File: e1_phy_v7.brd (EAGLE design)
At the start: 100 x 75 mm, 136 parts, among them IC2 LD117AS33TR, IC3 LD117AS33TR, IC4 MCP4725, U1 XRT82D20, U2 GPS_GNS_2201, U3 VCTCXO-CONNORWINFIELD, U4 VCXO_TAITIEN_VT, X2 SMA-142-0701-801/806, X3 JACK2.5_SJ-2523, X4 0446200002

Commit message: Pullup on i2c, ERASE jumper.
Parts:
- JP2: device jumper:JP1 -> jumper@1:JP1
- SV4: device con-lstb:MA08-2 -> con-lstb@1:MA08-2
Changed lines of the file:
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@@
 <?xml version="1.0" encoding="utf-8"?>
 <!DOCTYPE eagle SYSTEM "eagle.dtd">
-<eagle version="9.0.1">
+<eagle version="7.7.0">
 <drawing>
 <settings>
 <setting alwaysvectorfont="no"/>
-<setting keepoldvectorfont="yes"/>
 <setting verticaltext="up"/>
 </settings>
@@
 <attribute name="VALUE" x="43.65625" y="36.86175" size="0.0254" layer="27"/>
 </element>
-<element name="SV4" library="con-lstb" library_urn="urn:adsk.eagle:library:162" package="MA08-2" package3d_urn="urn:adsk.eagle:package:8335/1" value="" x="69.85" y="13.97" smashed="yes" rot="R90">
+<element name="SV4" library="con-lstb@1" package="MA08-2" value="" x="69.85" y="13.97" smashed="yes" rot="R90">
 <attribute name="MF" value="" x="69.85" y="13.97" size="1.778" layer="27" rot="R90" display="off"/>
 <attribute name="MPN" value="" x="69.85" y="13.97" size="1.778" layer="27" rot="R90" display="off"/>
@@
 <attribute name="TP_SIGNAL_NAME" value="" x="25.4" y="64.77" size="1.778" layer="27" font="vector" display="off"/>
 </element>
-<element name="X4" library="con-molex" library_urn="urn:adsk.eagle:library:165" package="0446200002" value="0446200002" x="4.7625" y="15.24" smashed="yes" rot="R270">
+<element name="X4" library="con-molex" package="0446200002" value="0446200002" x="4.7625" y="15.24" smashed="yes" rot="R270">
 <attribute name="MF" value="MOLEX" x="4.7625" y="15.24" size="1.778" layer="27" font="vector" rot="R270" display="off"/>
 <attribute name="MPN" value="0446200002" x="4.7625" y="15.24" size="1.778" layer="27" font="vector" rot="R270" display="off"/>
@@
 <attribute name="VALUE" x="60.6425" y="51.435" size="1.27" layer="27" rot="R90"/>
 </element>
-<element name="JP2" library="jumper" library_urn="urn:adsk.eagle:library:252" package="JP1" package3d_urn="urn:adsk.eagle:package:15455/1" value="" x="20.32" y="34.29" rot="R270"/>
+<element name="JP2" library="jumper@1" package="JP1" value="" x="20.32" y="34.29" rot="R270"/>
 </elements>
 <signals>
@@
 which will not be processed correctly with this version.
 </note>
-<note version="8.2" severity="warning">
-Since Version 8.2, EAGLE supports online libraries. The ids
-of those online libraries will not be understood (or retained)
-with this version.
-</note>
-<note version="8.3" severity="warning">
-Since Version 8.3, EAGLE supports URNs for individual library
-assets (packages, symbols, and devices). The URNs of those assets
-will not be understood (or retained) with this version.
-</note>
-<note version="8.3" severity="warning">
-Since Version 8.3, EAGLE supports the association of 3D packages
-with devices in libraries, schematics, and board files. Those 3D
-packages will not be understood (or retained) with this version.
-</note>
 </compatibility>

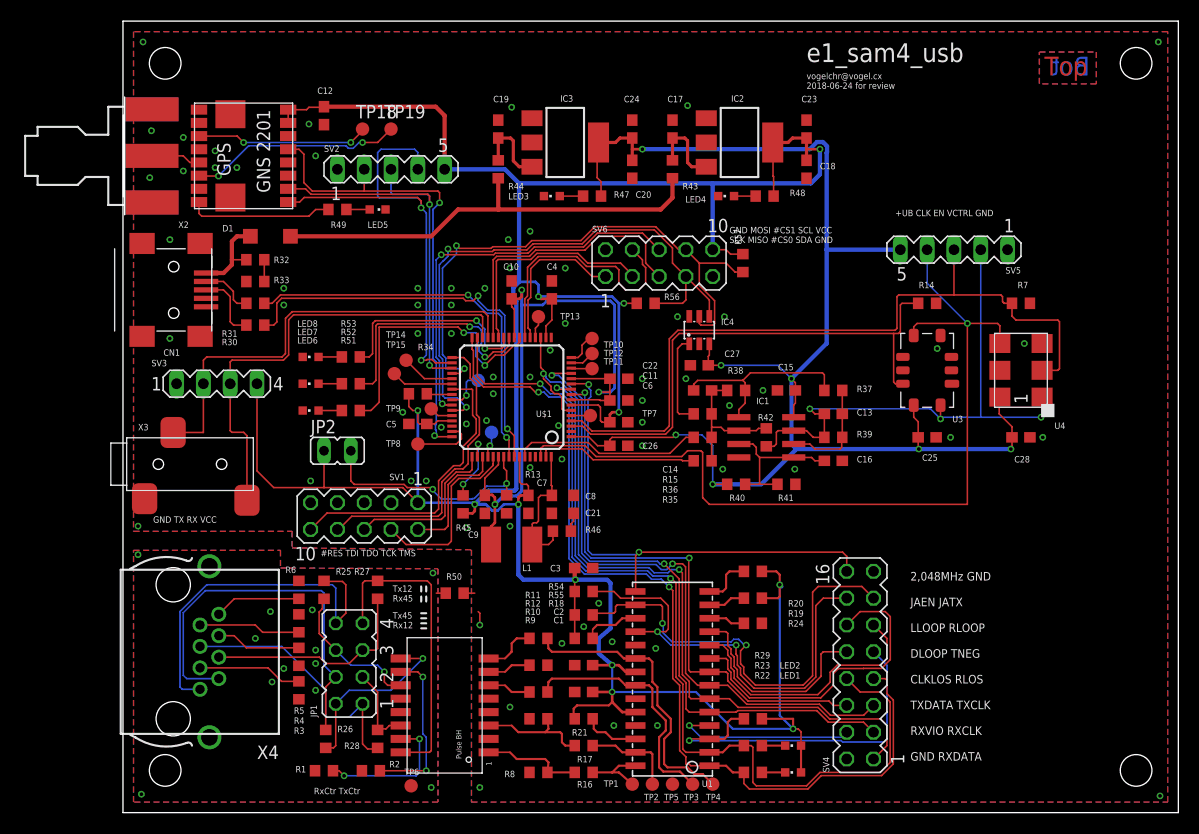
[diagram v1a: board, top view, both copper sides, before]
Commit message: Changed LIU to IDT82V2081.
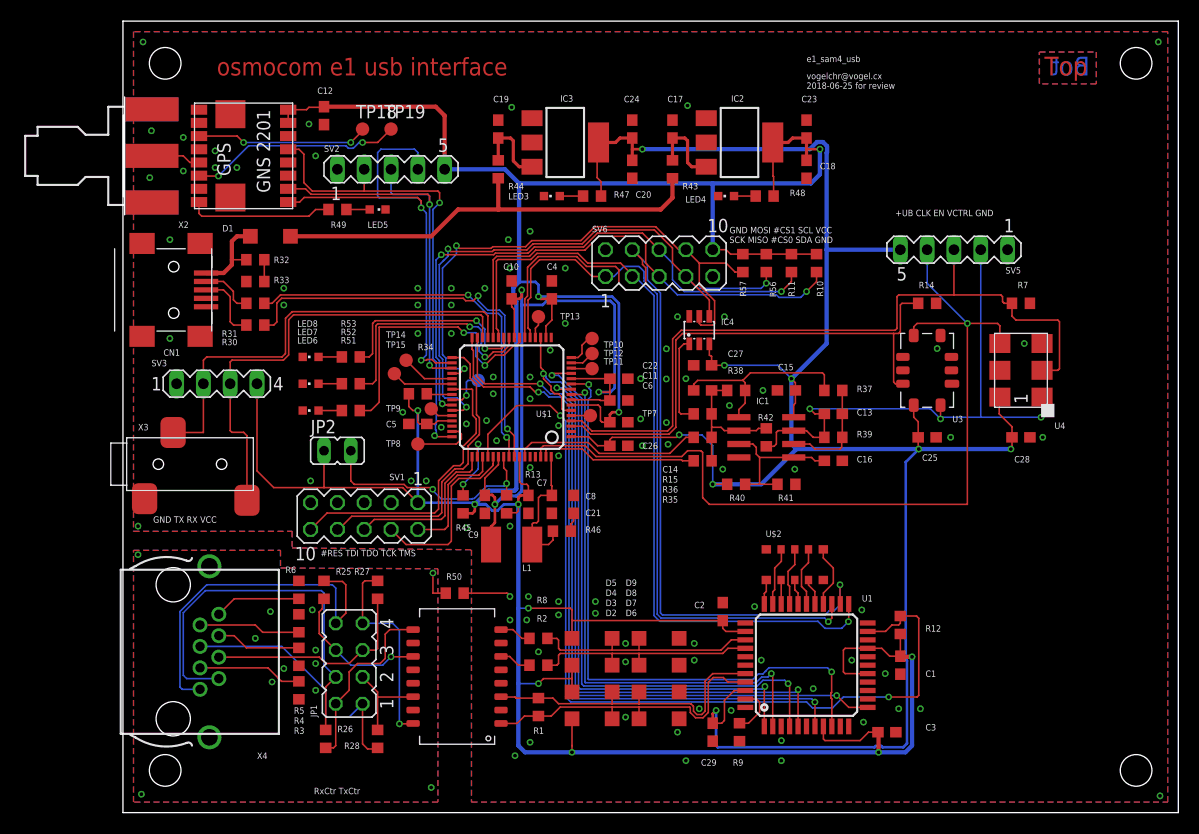
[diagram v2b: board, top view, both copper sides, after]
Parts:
- removed LED1, LED2: (no value), led:CHIPLED_0603
- removed R16, R17: 0R, rcl:R0603
- removed R18, R19, R20, R24: DNP, rcl:R0603
- removed R21, R22, R23, R29, R54, R55: 1k, rcl:R0603
- removed SV4: (no value), con-lstb@1:MA08-2
- removed TP1, TP17, TP2, TP3, TP4, TP5, TP6: TPB1,27, testpad:B1,27
- added C29: 100n, rcl:C0603
- added D2, D3, D4, D5, D6, D7, D8, D9: MBR0520LT, diode@1:SOD123
- added U$2: MNR 8x10k, laforge:MNR35
- C3: value 10u -> 100n
- R10, R11: value 9R1 -> 10k
- R12: value DNP -> 10k
- R8: value 60R -> DNP
- R9: value 60R -> 3k 1%
- TR1: value PE-65861 -> PULSE_T1094NL; device cvogel:PULSE_BH_XFORMER -> laforge:PULSE_BH
- U1: value XRT82D20 -> IDT82V2081; device cvogel:SOJ28/3 -> idt82v2081:TQFP44
- moved R10 48.4 mm to (65.7, 52.1), turned to 90 degrees
- moved R11 42.9 mm to (63.3, 52.1), turned to 90 degrees
- moved R12 34.5 mm to (73.7, 17.8), turned to 90 degrees
- moved C3 32.7 mm to (72.4, 7.62)
- moved C1 30.1 mm to (73.7, 14.0), turned to 270 degrees
- moved R1 21.2 mm to (39.4, 10.0), turned to 90 degrees
- moved R9 19.1 mm to (58.4, 7.62), turned to 270 degrees
- moved R2 18.8 mm to (39.4, 14.0), turned to 180 degrees
- moved C2 14.1 mm to (56.8, 19.1), turned to 90 degrees
- moved U1 12.8 mm to (64.8, 14.0)
- moved R8 12.7 mm to (39.4, 16.5)
- moved R56 12.0 mm to (61.0, 52.1), turned to 90 degrees
- moved TR1 2.77 mm to (31.6, 12.7), turned to 180 degrees
- moved C27 0.32 mm to (54.9, 42.4)
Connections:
- removed net #ATM: R24.1, U1.12
- removed net #CLKLOS: R23.1, SV4.8, U$1.31, U1.2
- removed net #DLOOP: SV4.10, U1.11
- removed net #LLOOP: SV4.12, U1.9
- removed net #RLOOP: SV4.11, U1.10
- removed net #RLOS: R22.1, SV4.7, U$1.32, U1.1
- removed net DIGI: R18.1, U1.17
- removed net JAEN: R54.2, SV4.14, U1.18
- removed net JATX: R55.2, SV4.13, U1.16
- removed net MUTERX: R21.1, U1.26
- removed net N$1: LED1.C, R22.2
- removed net N$2: LED2.C, R23.2
- removed net RAOS: R19.2, U1.13
- removed net RRING_LIU: R17.2, TP2.TP, U1.27
- removed net RTIP_LIU: R16.2, TP1.TP, U1.28
- removed net RX_PRI_CTR: R1.2, TR1.15
- removed net RX_VIOLATION: SV4.4, U1.4
- removed net TAOS: R20.2, U1.14
- removed net TNEG_CODE: R29.1, SV4.9, U1.3
- removed net TRING_XFMR: R11.1, TR1.8
- removed net TTIP_XFMR: R10.1, TR1.6
- removed net TX_PRI_CTR: R12.1, TR1.7
- removed net TX_SEC_CTR: R2.2, TR1.10
- new net #RST_LIU: U$1.31, U1.12
- new net #SPI_CS2: R11.1, SV6.6, U$1.42
- new net AD0: U$2.6, U1.26
- new net AD1: U$2.4, U1.27
- new net AD2: U$2.7, U1.28
- new net AD3: U$2.3, U1.29
- new net AD4: U$2.8, U1.30
- new net AD5: U$2.2, U1.31
- new net AD6: U$2.9, U1.32
- new net AD7: U$2.1, U1.33
- new net LOS_LIU: U$1.32, U1.7
- new net N$25: R8.2, TR1.8
- new net N$31: R9.1, U1.43
- net #SPI_CS0: now also R10.1
- net #SPI_CS1: now also R12.2, U$1.52, U1.21; no longer SV6.6, U$1.42
- net +UB: now also C29.1, U1.42
- net CLK2048: now also U1.9; no longer SV4.16, U1.15
- net GND: now also C29.2, D6.A, D7.A, D8.A, D9.A, U$2.10, U$2.5, U1.10, U1.11, U1.13, U1.14, U1.15, U1.17, U1.18, U1.22, U1.3, U1.38, U1.39, U1.44; no longer R12.2, R24.2, R8.2, SV4.15, SV4.2, TP5.TP, TR1.2, U1.19, U1.23, U1.25
- net GNDIO: no longer R1.1, R2.1, TP6.TP
- net N$5: now also R2.2, TR1.6; no longer TP17.TP, U$1.52
- net RRING: now also D3.A, D7.C, R1.2, U1.40; no longer R17.1, R9.1
- net RTIP: now also D2.A, D6.C, R1.1, U1.41; no longer R16.1, R8.1
- net RX_CLK: now also U1.4; no longer SV4.3, U1.5
- net RX_DATA: now also U1.5; no longer SV4.1, U1.6
- net SPI_MISO: now also U1.23
- net SPI_MOSI: now also U1.24
- net SPI_SCK: now also U1.25
- net TRING: now also D5.A, D9.C, R8.1, U1.36; no longer R11.2, TP4.TP, U1.20
- net TTIP: now also D4.A, D8.C, R2.1, U1.37; no longer R10.2, TP3.TP, U1.22
- net TX_CLK: now also U1.1; no longer SV4.5, U1.7
- net TX_DATA: now also U1.2; no longer SV4.6, U1.8
- net VCC: now also D2.C, D3.C, D4.C, D5.C, R10.2, R11.2, R12.1, U1.16, U1.19, U1.35, U1.8; no longer LED1.A, LED2.A, R18.2, R19.1, R20.1, R21.2, R29.2, R54.1, R55.1, U1.21, U1.24
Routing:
- net #CLKLOS: track 90.4 -> 0.00 mm, vias 2 -> 0
- net #RLOS: track 88.3 -> 0.00 mm, vias 2 -> 0
- net #RST_LIU: track 0.00 -> 69.8 mm, vias 0 -> 2
- net LOS_LIU: track 0.00 -> 67.3 mm, vias 0 -> 2
- net SPI_MOSI: track 24.4 -> 82.2 mm, vias 0 -> 1
- net +UB: track 140.7 -> 197.5 mm, vias 7 -> 8
- net SPI_SCK: track 14.8 -> 70.4 mm, vias 0 -> 1
- net #SPI_CS2: track 0.00 -> 54.1 mm, vias 0 -> 3
- net SPI_MISO: track 21.5 -> 75.5 mm, vias 0 -> 1
- net #SPI_CS1: track 37.7 -> 85.0 mm
- net JATX: track 43.2 -> 0.00 mm, vias 2 -> 0
- net JAEN: track 42.2 -> 0.00 mm, vias 2 -> 0
- net VCC: track 309.2 -> 347.7 mm, vias 12 -> 11
- net TNEG_CODE: track 34.5 -> 0.00 mm, vias 1 -> 0
- net #LLOOP: track 30.7 -> 0.00 mm
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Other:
- board text added: "osmocom e1 usb interface"
- board text added: "vogelchr@vogel.cx 2018-06-25 for review"
- board text removed: "2,048MHz GND JAEN JATX LLOOP RLOOP DLOOP TNEG CLKLOS RLOS TXDATA TXCLK RXVIO RXCLK GND RXDATA"
- board text removed: "Tx12 Rx45"
- board text removed: "Tx45 Rx12"
- board text removed: "vogelchr@vogel.cx 2018-06-24 for review"

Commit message: Regenerated v7 eagle files, made .pdf for schematic.
 -> next release candidate 20180703
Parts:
- removed IC4: MCP4725, dp_devices:SOT-23-6
- removed R32: 27k, rcl:R0603
- removed R33: 47k, rcl:R0603
- removed R56, R57: 10k, rcl:R0603
- removed SV6: (no value), con-lstb:MA05-2
- removed U$2: MNR 8x10k, laforge:MNR35
- added D10: 0603ESDA-TR, laforge:0603
- added L2: 10uH, rcl:L1812
- added RN1, RN2: (no value), resistor-dil:EXB38V
- added RN3, RN4: 10k, resistor-dil:EXB38V
- added SV4: (no value), con-lstb@1:MA06-1
- added U5, U7: IP4234CZ6, laforge:TSOP-6
- added U6: (no value), max5215_max5217:UMAX8
- R1: value DNP -> 120R
- R2, R8: value DNP -> 9R
- SV1: device con-lstb:MA05-2 -> con-lstb@1:MA05-2
- SV3: device con-lstb:MA04-1 -> con-lstb@1:MA10-2
- moved SV3 83.9 mm to (88.9, 15.2), turned to 270 degrees
- moved R10 49.7 mm to (18.9, 35.6)
- moved R11 47.5 mm to (80.0, 7.62), turned to 270 degrees
- moved SV1 36.8 mm to (50.8, 52.1), turned to 0 degrees
- moved LED6 15.3 mm to (2.54, 36.8)
- moved LED7 15.3 mm to (2.54, 39.4)
- moved LED8 15.3 mm to (2.54, 41.9)
- moved R52 15.3 mm to (6.35, 39.4)
- moved R53 15.3 mm to (6.35, 41.9)
- moved R51 12.8 mm to (8.89, 36.8)
- moved L1 11.1 mm to (47.3, 29.2), turned to 270 degrees
- moved JP2 9.92 mm to (26.7, 26.7), turned to 90 degrees
- moved R30 7.79 mm to (19.8, 48.9)
- moved C27 4.42 mm to (59.1, 44.0), turned to 180 degrees
- moved R31 4.34 mm to (16.5, 50.0)
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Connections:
- net USB_VBUS_CON renamed USB_VBUS
- removed net LOS_LIU: U$1.32, U1.7
- removed net N$12: CN1.VBUS, D1.A, R32.2
- removed net USB_VBUS_SENS: R32.1, R33.2
- new net #LIU_INT: U$1.32, U1.20
- new net LIU_VDDA: C29.1, L2.2, U1.42
- new net N$1: CN1.D+, U5.1
- new net N$2: CN1.D-, U5.6
- new net N$32: SV4.2, SV4.6
- new net URXD0_SAMBA_RX_CON: R10.1, SV4.4, U7.6, X3.2
- new net UTXD0_SAMBA_TX_CON: SV4.5, U7.1, X3.3
- new net VBUS_CONN: CN1.VBUS, D1.A, U5.5
- net #RESET: now also RN4.4, SV3.15; no longer SV1.10
- net #RST_LIU: now also R11.1
- net #SPI_CS0: now also RN3.2, SV1.10; no longer R10.1, SV6.5
- net #SPI_CS2: now also RN3.4, SV1.4; no longer R11.1, SV6.6
- net +UB: now also U6.1, U6.7; no longer C29.1, IC4.3, U1.42
- net AD0: now also RN2.8; no longer U$2.6
- net AD1: now also RN2.7; no longer U$2.4
- net AD2: now also RN2.6; no longer U$2.7
- net AD3: now also RN2.5; no longer U$2.3
- net AD4: now also RN1.4; no longer U$2.8
- net AD5: now also RN1.3; no longer U$2.2
- net AD6: now also RN1.2; no longer U$2.9
- net AD7: now also RN1.1; no longer U$2.1
- net DAC_I2C: now also U6.6; no longer IC4.1
- net GND: now also D10.2, RN1.5, RN1.6, RN1.7, RN1.8, RN2.1, RN2.2, RN2.3, RN2.4, SV1.2, SV3.10, SV3.12, SV3.14, SV3.16, SV3.18, SV3.20, SV3.4, SV3.6, SV3.8, SV4.1, U5.2, U6.8, U7.2; no longer IC4.2, IC4.6, R33.1, SV1.3, SV1.5, SV1.9, SV3.1, SV6.2, SV6.9, U$2.10, U$2.5
- net I2C_SCL: now also RN3.3, SV1.5, U6.3; no longer IC4.5, R57.1, SV6.8
- net I2C_SDA: now also RN3.1, SV1.6, U6.4; no longer IC4.4, R56.1, SV6.7
- net N$4: now also D10.1
- net SPI_MISO: now also SV1.7; no longer SV6.3
- net SPI_MOSI: now also SV1.8; no longer SV6.4
- net SPI_SCK: now also SV1.9; no longer SV6.1
- net TCK_SWDCLK: now also RN4.2, SV3.9; no longer SV1.4
- net TDI: now also SV3.5; no longer SV1.8
- net TDO: now also SV3.13; no longer SV1.6
- net TMS_SWDIO: now also RN4.1, SV3.7; no longer SV1.2
- net URXD0_SAMBA_RX: now also U7.4; no longer SV3.3, X3.2
- net USB_DDM_CON: now also U5.4; no longer CN1.D-
- net USB_DDP_CON: now also U5.3; no longer CN1.D+
- net UTXD0_SAMBA_TX: now also U7.3; no longer SV3.2, X3.3
- net VCC: now also L2.1, RN3.5, RN3.6, RN3.7, RN3.8, RN4.5, RN4.6, RN4.7, RN4.8, SV3.1, U7.5; no longer R56.2, R57.2, SV3.4, SV6.10
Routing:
- net VCC: track 347.7 -> 432.7 mm, vias 11 -> 15
- net #LIU_INT: track 0.00 -> 78.0 mm, vias 0 -> 2
- net #RESET: track 28.2 -> 102.9 mm
- net TMS_SWDIO: track 12.1 -> 81.0 mm
- net TCK_SWDCLK: track 17.3 -> 85.4 mm, vias 0 -> 1
- net LOS_LIU: track 67.3 -> 0.00 mm, vias 2 -> 0
- net TDO: track 15.6 -> 79.8 mm
- net TDI: track 28.9 -> 80.8 mm, vias 0 -> 1
- net +UB: track 197.5 -> 146.1 mm, vias 8 -> 9
- net UTXD0_SAMBA_TX_CON: track 0.00 -> 31.8 mm
- net URXD0_SAMBA_RX: track 44.2 -> 21.0 mm, vias 0 -> 2
- net UTXD0_SAMBA_TX: track 42.8 -> 20.4 mm
- net URXD0_SAMBA_RX_CON: track 0.00 -> 21.4 mm
- net LED3: track 19.8 -> 40.4 mm
- net LED2: track 23.5 -> 39.9 mm
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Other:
- board text added: "ERASE"
- board text added: "GND - - RxD TxD -"
- board text added: "vogelchr@vogel.cx 2018-07-03 for review"
- board text removed: "#RES TDI TDO TCK TMS"
- board text removed: "GND MOSI #CS1 SCL VCC SCK MISO #CS0 SDA GND"
- board text removed: "GND TX RX VCC"
- board text removed: "vogelchr@vogel.cx 2018-06-25 for review"
